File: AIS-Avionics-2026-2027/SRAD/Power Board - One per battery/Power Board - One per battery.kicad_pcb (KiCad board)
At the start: 2 copper layers, 112.5 x 37.5 mm, 3 parts, among them J1 Conn_01x02, J2 Conn_01x02

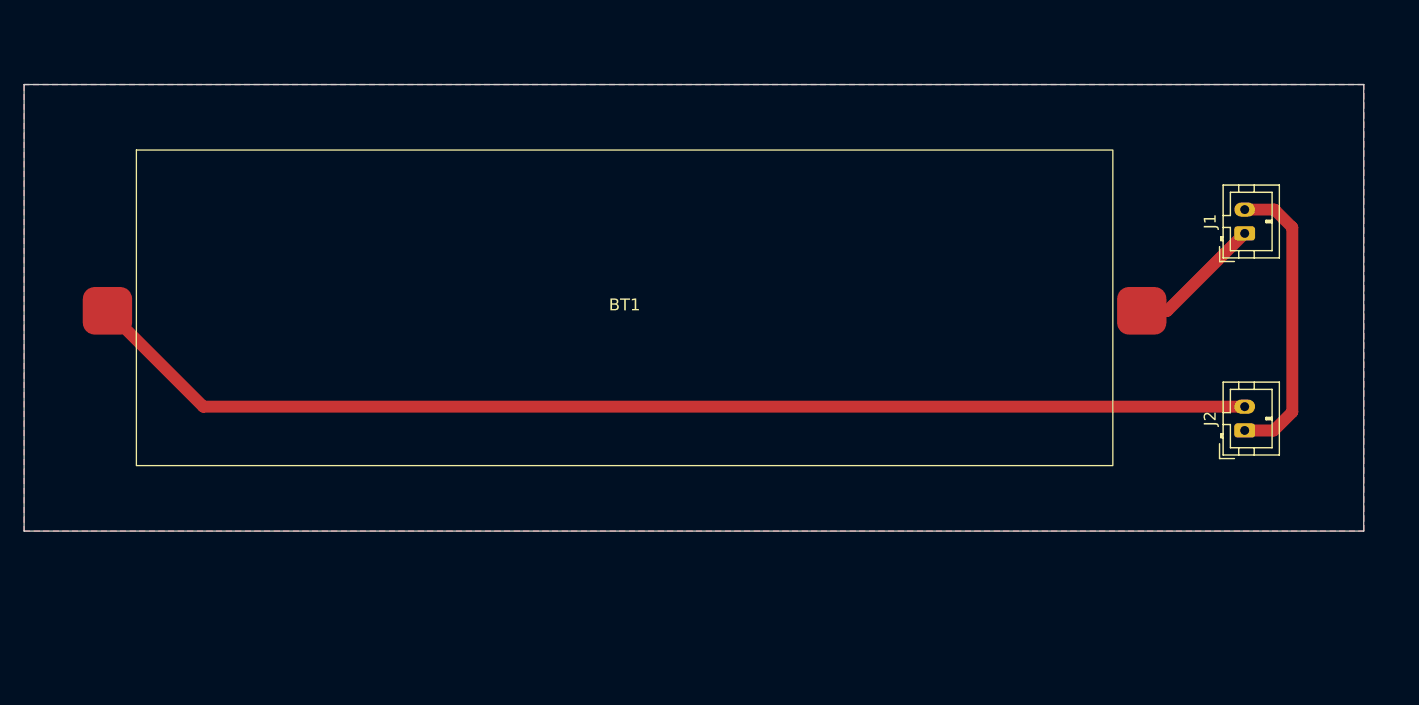
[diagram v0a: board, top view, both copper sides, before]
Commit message: Updated SRAD power board for singular component
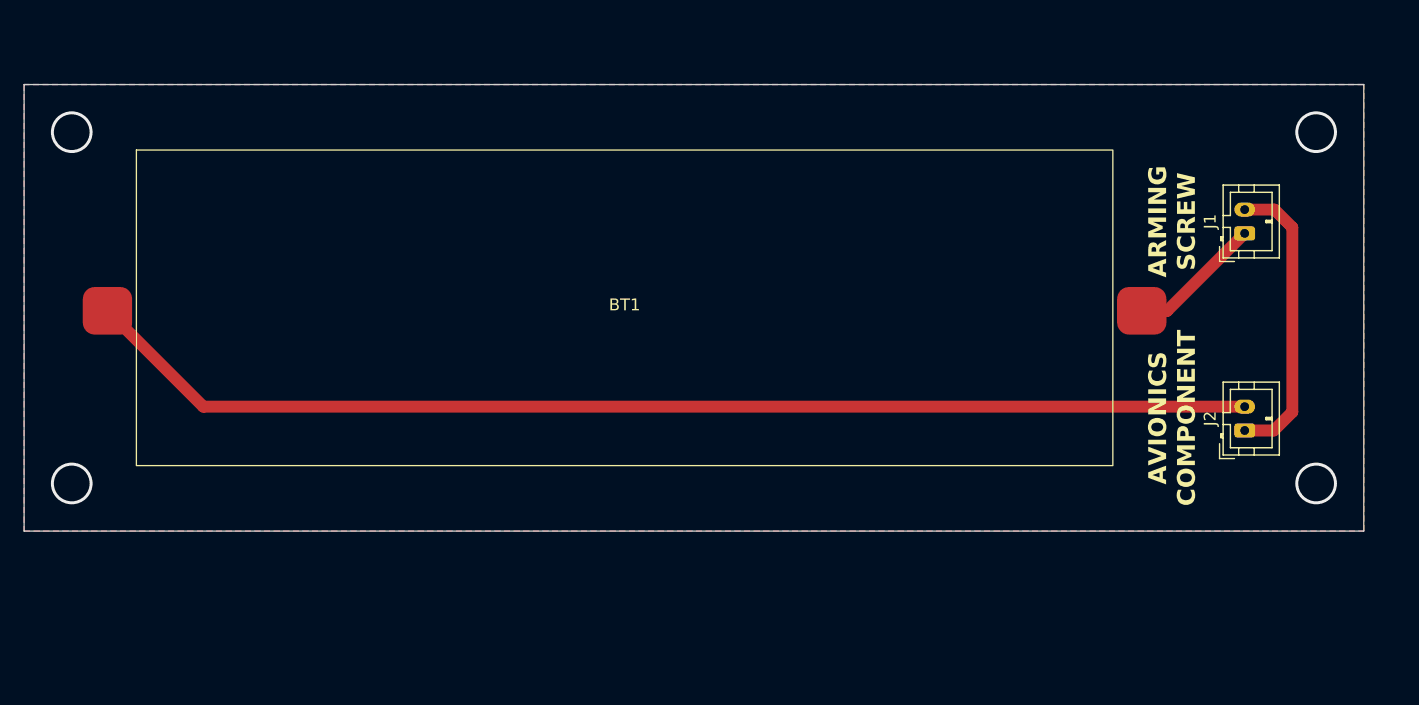
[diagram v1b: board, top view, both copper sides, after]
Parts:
- J1, J2: footprint Connector_JST:JST_PH_B2B-PH-K_1x02_P2.00mm_Vertical -> Reconfigured Standard Components:JST_PH_B2B-PH-K_1x02_P2.00mm_Vertical_CAD_Fixed
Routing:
- net (no net): vias 0 -> 4
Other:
- board text added: "ARMING SCREW"
- board text added: "AVIONICS COMPONENT"
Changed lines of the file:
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@@
 	(net 2 "Net-(BT1--)")
 	(net 3 "Net-(BT1-+)")
-	(footprint "Connector_JST:JST_PH_B2B-PH-K_1x02_P2.00mm_Vertical"
+	(footprint "Reconfigured Standard Components:JST_PH_B2B-PH-K_1x02_P2.00mm_Vertical_CAD_Fixed"
 		(layer "F.Cu")
 		(at 187.5 74.05 90)
@@
 			)
 		)
-		(property "Footprint" "Connector_JST:JST_PH_B2B-PH-K_1x02_P2.00mm_Vertical"
+		(property "Footprint" "Reconfigured Standard Components:JST_PH_B2B-PH-K_1x02_P2.00mm_Vertical_CAD_Fixed"
 			(at 0 0 90)
 			(unlocked yes)
@@
 			(pintype "passive")
 		)
-		(model "${KICAD8_3DMODEL_DIR}/Connector_JST.3dshapes/JST_PH_B2B-PH-K_1x02_P2.00mm_Vertical.wrl"
+		(model "${KICAD8_3DMODEL_DIR}/JST - PH - Thru (V) - 2Pin - 2.00mm.stp"
 			(offset
-				(xyz 0 0 0)
+				(xyz 1 0 0)
 			)
 			(scale
@@
 			)
 			(rotate
-				(xyz 0 0 0)
+				(xyz 0 0 180)
 			)
 		)
@@
 		)
 	)
-	(footprint "Connector_JST:JST_PH_B2B-PH-K_1x02_P2.00mm_Vertical"
+	(footprint "Reconfigured Standard Components:JST_PH_B2B-PH-K_1x02_P2.00mm_Vertical_CAD_Fixed"
 		(layer "F.Cu")
 		(at 187.5 57.5 90)
@@
 			)
 		)
-		(property "Footprint" "Connector_JST:JST_PH_B2B-PH-K_1x02_P2.00mm_Vertical"
+		(property "Footprint" "Reconfigured Standard Components:JST_PH_B2B-PH-K_1x02_P2.00mm_Vertical_CAD_Fixed"
 			(at 0 0 90)
 			(unlocked yes)
@@
 			(pintype "passive")
 		)
-		(model "${KICAD8_3DMODEL_DIR}/Connector_JST.3dshapes/JST_PH_B2B-PH-K_1x02_P2.00mm_Vertical.wrl"
+		(model "${KICAD8_3DMODEL_DIR}/JST - PH - Thru (V) - 2Pin - 2.00mm.stp"
 			(offset
-				(xyz 0 0 0)
+				(xyz 1 0 0)
 			)
 			(scale
@@
 			)
 			(rotate
-				(xyz 0 0 0)
-			)
-		)
+				(xyz 0 0 180)
+			)
+		)
+	)
+	(gr_rect
+		(start 89 49)
+		(end 193.5 78.5)
+		(stroke
+			(width 0.1)
+			(type default)
+		)
+		(fill none)
+		(layer "B.SilkS")
 	)
 	(gr_line
@@
 		(layer "Edge.Cuts")
 	)
+	(gr_text "ARMING\nSCREW"
+		(at 183.5 56.5 90)
+		(layer "F.SilkS")
+		(effects
+			(font
+				(size 1.5 1.5)
+				(thickness 0.3)
+				(bold yes)
+			)
+			(justify bottom)
+		)
+	)
+	(gr_text "AVIONICS\nCOMPONENT"
+		(at 183.5 73 90)
+		(layer "F.SilkS")
+		(effects
+			(font
+				(size 1.5 1.5)
+				(thickness 0.3)
+				(bold yes)
+			)
+			(justify bottom)
+		)
+	)
+	(via
+		(at 193.5 78.5)
+		(size 3.5)
+		(drill 3)
+		(layers "F.Cu" "B.Cu")
+		(net 0)
+	)
+	(via
+		(at 89 49)
+		(size 3.5)
+		(drill 3)
+		(layers "F.Cu" "B.Cu")
+		(net 0)
+	)
+	(via
+		(at 193.5 49)
+		(size 3.5)
+		(drill 3)
+		(layers "F.Cu" "B.Cu")
+		(net 0)
+	)
+	(via
+		(at 89 78.5)
+		(size 3.5)
+		(drill 3)
+		(layers "F.Cu" "B.Cu")
+		(net 0)
+	)
 	(segment

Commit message: Battery shenanigans.
So many battery shenanigans
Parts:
- added D1: D, Package_TO_SOT_THT:TO-264-2_Vertical, F.Cu at (137.6, 84.6)
- added F1: Fuse, Fuse:Fuseholder_Littelfuse_445_030_series_5x30mm, F.Cu at (159.0, 84.5)
- J1, J2: value Conn_01x02 -> Conn_01x02_Pin; footprint Reconfigured Standard Components:JST_PH_B2B-PH-K_1x02_P2.00mm_Vertical_CAD_Fixed -> Connector_JST:JST_PH_B2B-PH-K_1x02_P2.00mm_Vertical
- moved J2 85.0 mm to (103.2, 84.6), turned to 0 degrees
- moved J1 69.0 mm to (124.0, 84.6), turned to 0 degrees
- moved BT1 11.2 mm to (146.6, 63.5)
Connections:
- J1 pad 1: Net-(BT1-+) -> Net-(J1-Pin_1)
- J1 pad 2: Net-(J1-Pin_2) -> Net-(D1-K)
- J2 pad 1: Net-(J1-Pin_2) -> Net-(BT1--)
- J2 pad 2: Net-(BT1--) -> Net-(J1-Pin_1)
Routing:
- net Net-(BT1--): track 98.8 -> 21.1 mm
- net Net-(J1-Pin_2): track 24.8 -> 0.00 mm
- net Net-(J1-Pin_1): track 0.00 -> 18.8 mm
- net Net-(D1-A): track 0.00 -> 15.8 mm
- net Net-(BT1-+): track 11.3 -> 26.2 mm
- net Net-(D1-K): track 0.00 -> 11.6 mm
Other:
- board size 112.5 x 37.5 mm -> 105 x 55 mm
